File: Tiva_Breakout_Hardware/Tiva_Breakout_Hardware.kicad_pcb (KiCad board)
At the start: 2 copper layers, 146.1 x 69.8 mm, 61 parts, among them U1 TM4C129E_Launchpad

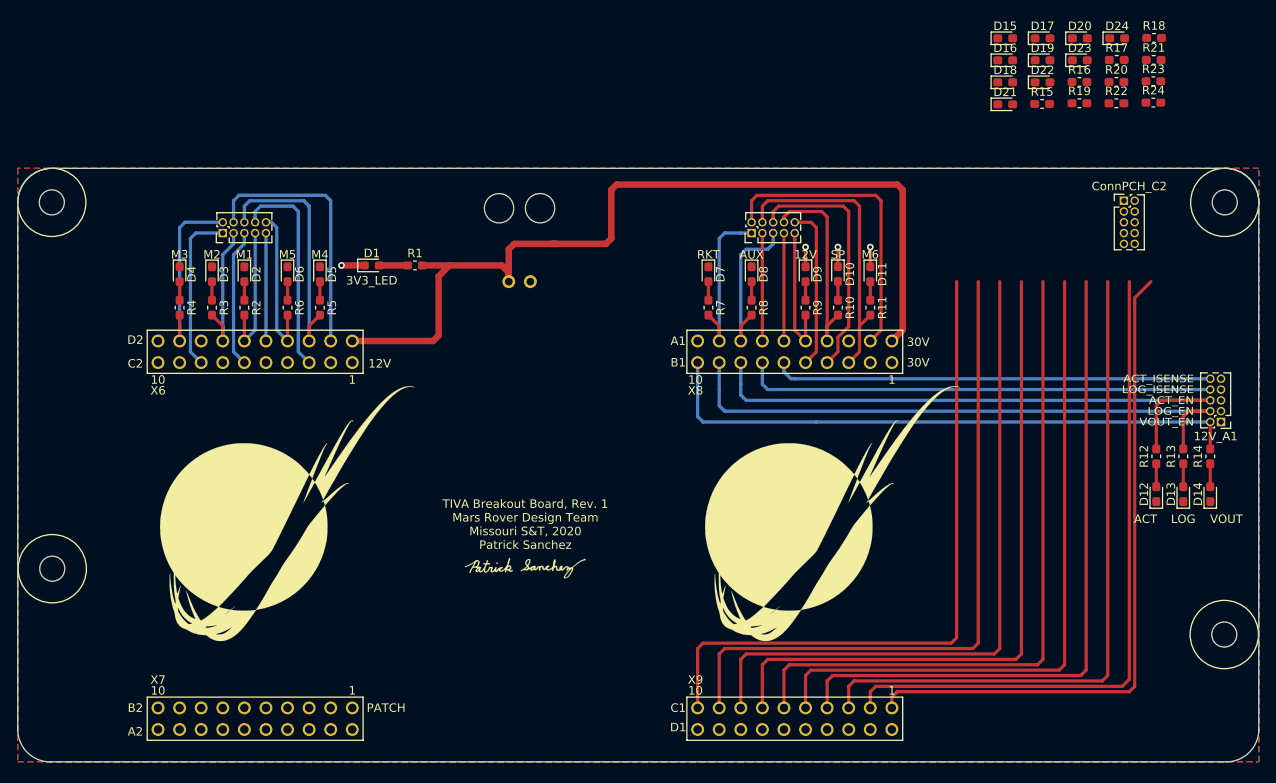
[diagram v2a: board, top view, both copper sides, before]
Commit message: Finished all wiring and LEDs, need resizing and silkscreen
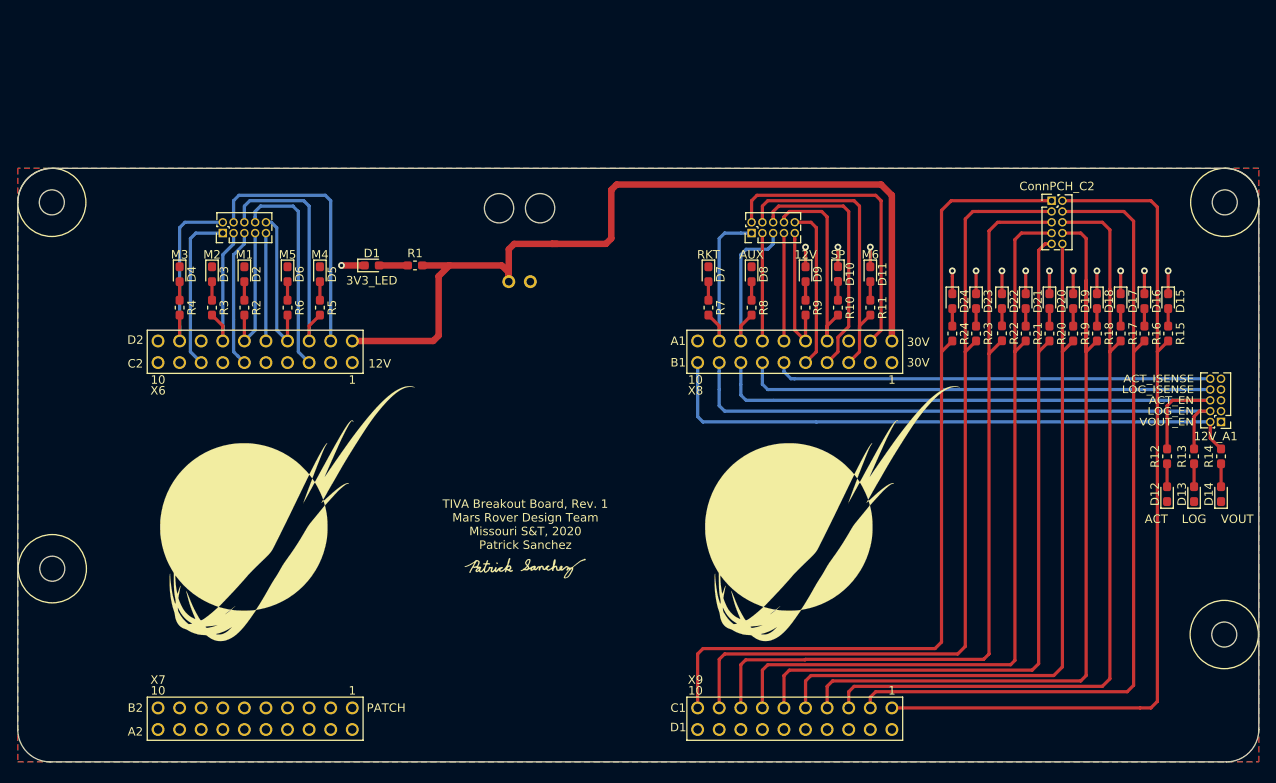
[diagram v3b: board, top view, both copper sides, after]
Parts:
- moved D24 36.5 mm to (194.5, 90.9), turned to 270 degrees
- moved D15 36.4 mm to (219.9, 90.9), turned to 270 degrees
- moved R23 36.3 mm to (197.3, 94.8), turned to 270 degrees
- moved R24 36.0 mm to (194.5, 94.8), turned to 270 degrees
- moved R21 35.5 mm to (203.1, 94.8), turned to 270 degrees
- moved R18 35.4 mm to (211.5, 94.8), turned to 270 degrees
- moved D16 32.7 mm to (217.1, 90.9), turned to 270 degrees
- moved D17 32.3 mm to (214.3, 90.9), turned to 270 degrees
- moved R17 32.2 mm to (214.3, 94.8), turned to 270 degrees
- moved D20 31.1 mm to (205.9, 90.9), turned to 270 degrees
- moved D23 30.9 mm to (197.3, 90.9), turned to 270 degrees
- moved R15 30.8 mm to (219.9, 94.8), turned to 270 degrees
- moved R20 30.6 mm to (205.9, 94.8), turned to 270 degrees
- moved R16 30.6 mm to (217.1, 94.8), turned to 270 degrees
- moved R22 30.2 mm to (200.4, 94.7), turned to 270 degrees
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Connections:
- ConnPCH_C2 pad 1: PATCH10_EN -> PATCH1_EN
- ConnPCH_C2 pad 10: PATCH5_EN -> PATCH6_EN
- ConnPCH_C2 pad 2: PATCH1_EN -> PATCH10_EN
- ConnPCH_C2 pad 3: PATCH9_EN -> PATCH2_EN
- ConnPCH_C2 pad 4: PATCH2_EN -> PATCH9_EN
- ConnPCH_C2 pad 5: PATCH8_EN -> PATCH3_EN
- ConnPCH_C2 pad 6: PATCH3_EN -> PATCH8_EN
- ConnPCH_C2 pad 7: PATCH7_EN -> PATCH4_EN
- ConnPCH_C2 pad 8: PATCH4_EN -> PATCH7_EN
- ConnPCH_C2 pad 9: PATCH6_EN -> PATCH5_EN
- R15 pad 2: PATCH1_EN -> PATCH10_EN
- R16 pad 2: PATCH2_EN -> PATCH9_EN
- R17 pad 2: PATCH3_EN -> PATCH8_EN
- R18 pad 2: PATCH4_EN -> PATCH7_EN
- R19 pad 2: PATCH5_EN -> PATCH6_EN
- R20 pad 2: PATCH6_EN -> PATCH5_EN
- R21 pad 2: PATCH7_EN -> PATCH4_EN
- R22 pad 2: PATCH8_EN -> PATCH3_EN
- R23 pad 2: PATCH9_EN -> PATCH2_EN
- R24 pad 2: PATCH10_EN -> PATCH1_EN
- U1 pad PF1: PATCH1_EN -> PATCH10_EN
- U1 pad PF2: PATCH2_EN -> PATCH9_EN
- U1 pad PF3: PATCH3_EN -> PATCH8_EN
- U1 pad PG0: PATCH4_EN -> PATCH7_EN
- U1 pad PL0: PATCH7_EN -> PATCH4_EN
- U1 pad PL1: PATCH8_EN -> PATCH3_EN
- U1 pad PL2: PATCH9_EN -> PATCH2_EN
- U1 pad PL3: PATCH10_EN -> PATCH1_EN
- U1 pad PL4: PATCH5_EN -> PATCH6_EN
- U1 pad PL5: PATCH6_EN -> PATCH5_EN
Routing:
- net GND: track 9.62 -> 36.6 mm, vias 4 -> 14
- net PATCH10_EN: track 79.9 -> 103.0 mm
- net PATCH1_EN: track 78.8 -> 101.7 mm
- net PATCH7_EN: track 79.9 -> 98.2 mm
- net PATCH9_EN: track 79.9 -> 98.1 mm
- net PATCH2_EN: track 79.8 -> 97.9 mm
- net PATCH3_EN: track 79.9 -> 94.5 mm
- net PATCH8_EN: track 79.9 -> 93.9 mm
- net PATCH4_EN: track 79.9 -> 90.6 mm
- net PATCH5_EN: track 79.9 -> 86.6 mm
- net PATCH6_EN: track 79.9 -> 85.7 mm
- net +3V3: track 106.7 -> 104.5 mm
- net Net-(D24-Pad2): track 0.00 -> 2.06 mm
- net Net-(D23-Pad2): track 0.00 -> 2.06 mm
- net Net-(D21-Pad2): track 0.00 -> 2.06 mm
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
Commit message: Finished layout, minus some silk screen stuff
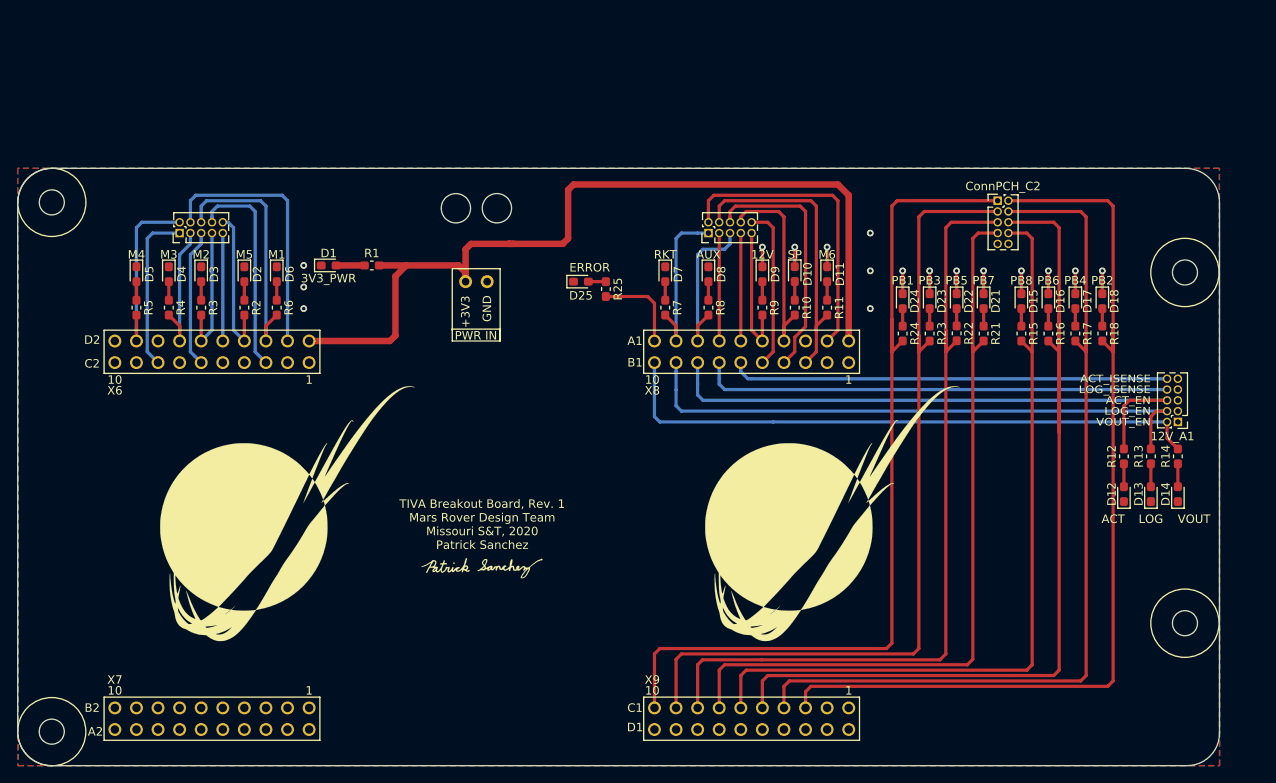
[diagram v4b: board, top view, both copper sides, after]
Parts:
- removed D19, D20: 3V3_LED, LED_SMD:LED_0603_1608Metric_Pad1.05x0.95mm_HandSolder
- removed R19, R20: 330, Resistor_SMD:R_0603_1608Metric_Pad1.05x0.95mm_HandSolder
- removed the REF** at (88.6, 122.4)
- removed the REF** at (226.5, 130.2)
- added D25: 3V3_LED, LED_SMD:LED_0603_1608Metric_Pad1.05x0.95mm_HandSolder, F.Cu at (150.8, 88.6)
- added R25: 330, Resistor_SMD:R_0603_1608Metric_Pad1.05x0.95mm_HandSolder, F.Cu at (153.7, 89.5)
- added REF**: 4_40_Hole, MRDT_Drill_Holes:4_40_Hole, F.Cu at (221.9, 128.8)
- added REF**: 4_40_Hole, MRDT_Drill_Holes:4_40_Hole, F.Cu at (221.9, 87.6)
- moved REF** 162.1 mm to (84.5, 145.6), turned to 0 degrees
- moved D5 21.6 mm to (98.5, 87.8)
- moved R5 21.6 mm to (98.5, 91.7)
- moved D15 17.3 mm to (202.6, 90.9)
- moved R15 17.3 mm to (202.6, 94.8)
- moved D16 11.3 mm to (205.8, 90.9)
- moved R16 11.3 mm to (205.8, 94.8)
- moved ConnPCH_C2 6.35 mm to (199.8, 79.1)
- moved D24 5.84 mm to (188.7, 90.9)
- moved R24 5.84 mm to (188.7, 94.8)
- moved D23 5.46 mm to (191.8, 90.9)
- moved R23 5.46 mm to (191.8, 94.8)
- moved D17 5.33 mm to (209.0, 90.9)
- moved D22 5.33 mm to (195.0, 90.9)
- moved R17 5.33 mm to (209.0, 94.8)
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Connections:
- net PATCH1_EN renamed PB1_EN
- net PATCH2_EN renamed PB3_EN
- net PATCH3_EN renamed PB5_EN
- net PATCH4_EN renamed PB7_EN
- Conn30V_L1 pad 10: M5_EN -> M1_EN
- Conn30V_L1 pad 2: M3_EN -> M4_EN
- Conn30V_L1 pad 3: M2_EN -> M3_EN
- Conn30V_L1 pad 6: M4_EN -> M5_EN
- Conn30V_L1 pad 7: M1_EN -> M2_EN
- Conn30V_R1 pad 10: 12V_ISENSE -> SP_ISENSE
- Conn30V_R1 pad 2: M6_ISENSE -> RKT_ISENSE
- Conn30V_R1 pad 3: RKT_ISENSE -> AUX_ISENSE
- Conn30V_R1 pad 6: SP_ISENSE -> M6_ISENSE
- Conn30V_R1 pad 7: AUX_ISENSE -> 12V_ISENSE
- ConnPCH_C2 pad 10: PATCH6_EN -> GND
- ConnPCH_C2 pad 2: PATCH10_EN -> PB2_EN
- ConnPCH_C2 pad 4: PATCH9_EN -> PB4_EN
- ConnPCH_C2 pad 6: PATCH8_EN -> PB6_EN
- ConnPCH_C2 pad 8: PATCH7_EN -> PB8_EN
- ConnPCH_C2 pad 9: PATCH5_EN -> GND
- R15 pad 2: PATCH10_EN -> PB8_EN
- R16 pad 2: PATCH9_EN -> PB6_EN
- R17 pad 2: PATCH8_EN -> PB4_EN
- R18 pad 2: PATCH7_EN -> PB2_EN
- U1 pad PB3: Net-(U1-PadPB3) -> ERROR
- U1 pad PD3: RKT_ISENSE -> AUX_ISENSE
- U1 pad PD5: M1_EN -> M2_EN
- U1 pad PE1: SP_ISENSE -> M6_ISENSE
- U1 pad PE2: 12V_ISENSE -> SP_ISENSE
- U1 pad PE4: M6_ISENSE -> RKT_ISENSE
- U1 pad PE5: AUX_ISENSE -> 12V_ISENSE
- U1 pad PF1: PATCH10_EN -> Net-(U1-PadPF1)
- U1 pad PF2: PATCH9_EN -> Net-(U1-PadPF2)
- U1 pad PF3: PATCH8_EN -> PB2_EN
- U1 pad PG0: PATCH7_EN -> PB4_EN
- U1 pad PL4: PATCH6_EN -> PB6_EN
- U1 pad PL5: PATCH5_EN -> PB8_EN
- U1 pad PN5: M3_EN -> M4_EN
- U1 pad PP0: M4_EN -> M5_EN
- U1 pad PP1: M5_EN -> M1_EN
- U1 pad PQ0: M2_EN -> M3_EN
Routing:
- net PB6_EN: track 0.00 -> 117.1 mm
- net PB2_EN: track 0.00 -> 111.4 mm
- net PB4_EN: track 0.00 -> 105.1 mm
- net PATCH10_EN: track 103.0 -> 0.00 mm
- net PATCH7_EN: track 98.2 -> 0.00 mm
- net PATCH9_EN: track 98.1 -> 0.00 mm
- net PATCH8_EN: track 93.9 -> 0.00 mm
- net PB8_EN: track 0.00 -> 93.6 mm
- net PATCH5_EN: track 86.6 -> 0.00 mm
- net PATCH6_EN: track 85.7 -> 0.00 mm
- net RKT_ISENSE: track 12.7 -> 35.3 mm
- net M5_EN: track 18.4 -> 29.5 mm
- net ERROR: track 0.00 -> 10.5 mm
- net SP_ISENSE: track 29.5 -> 19.2 mm
- net GND: track 36.6 -> 28.5 mm, vias 14 -> 17
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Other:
- board size 146.1 x 69.8 mm -> 141.4 x 70.3 mm
- board text added: "3V3_PWR"
- board text added: "ERROR"
- board text added: "PB1"
- board text added: "PB2"
- board text added: "PB3"
- board text added: "PB4"
- board text added: "PB5"
- board text added: "PB6"
- board text added: "PB7"
- board text added: "PB8"
- board text removed: "30V"
- board text removed: "3V3_LED"
- board text removed: "ACT_CRRT"
- board text removed: "ACT_CTRL"
- board text removed: "LOG_CRRT"
- board text removed: "LOG_CTRL"
- board text removed: "PATCH"

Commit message: Added pulldown resistors & LED colors
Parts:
- added R19: 10k, Resistor_SMD:R_0603_1608Metric_Pad1.05x0.95mm_HandSolder, F.Cu at (188.7, 121.4)
- added R20: 10k, Resistor_SMD:R_0603_1608Metric_Pad1.05x0.95mm_HandSolder, F.Cu at (191.8, 121.4)
- added R26: 10k, Resistor_SMD:R_0603_1608Metric_Pad1.05x0.95mm_HandSolder, F.Cu at (195.0, 121.4)
- added R27: 10k, Resistor_SMD:R_0603_1608Metric_Pad1.05x0.95mm_HandSolder, F.Cu at (198.2, 121.4)
- added R28: 10k, Resistor_SMD:R_0603_1608Metric_Pad1.05x0.95mm_HandSolder, F.Cu at (212.2, 121.4)
- added R29: 10k, Resistor_SMD:R_0603_1608Metric_Pad1.05x0.95mm_HandSolder, F.Cu at (209.0, 121.4)
- added R30: 10k, Resistor_SMD:R_0603_1608Metric_Pad1.05x0.95mm_HandSolder, F.Cu at (205.8, 121.4)
- added R31: 10k, Resistor_SMD:R_0603_1608Metric_Pad1.05x0.95mm_HandSolder, F.Cu at (202.6, 121.4)
- D1: value 3V3_LED -> GRN
- D10, D11, D12, D13, D14, D15, D16, D17, D18, D2, D21, D22, D23, D24, D3, D4, D5, D6, D7, D8, D9: value 3V3_LED -> BLU
- D25: value 3V3_LED -> RED
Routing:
- net GND: track 28.5 -> 45.0 mm, vias 17 -> 25
- net PB8_EN: track 93.6 -> 95.4 mm
- net PB7_EN: track 90.0 -> 91.8 mm
- net PB4_EN: track 105.1 -> 106.9 mm
- net PB3_EN: track 98.9 -> 100.6 mm
- net PB2_EN: track 111.4 -> 113.2 mm
- net PB1_EN: track 104.6 -> 106.4 mm
- net PB6_EN: track 117.1 -> 118.9 mm
- net PB5_EN: track 95.7 -> 97.5 mm

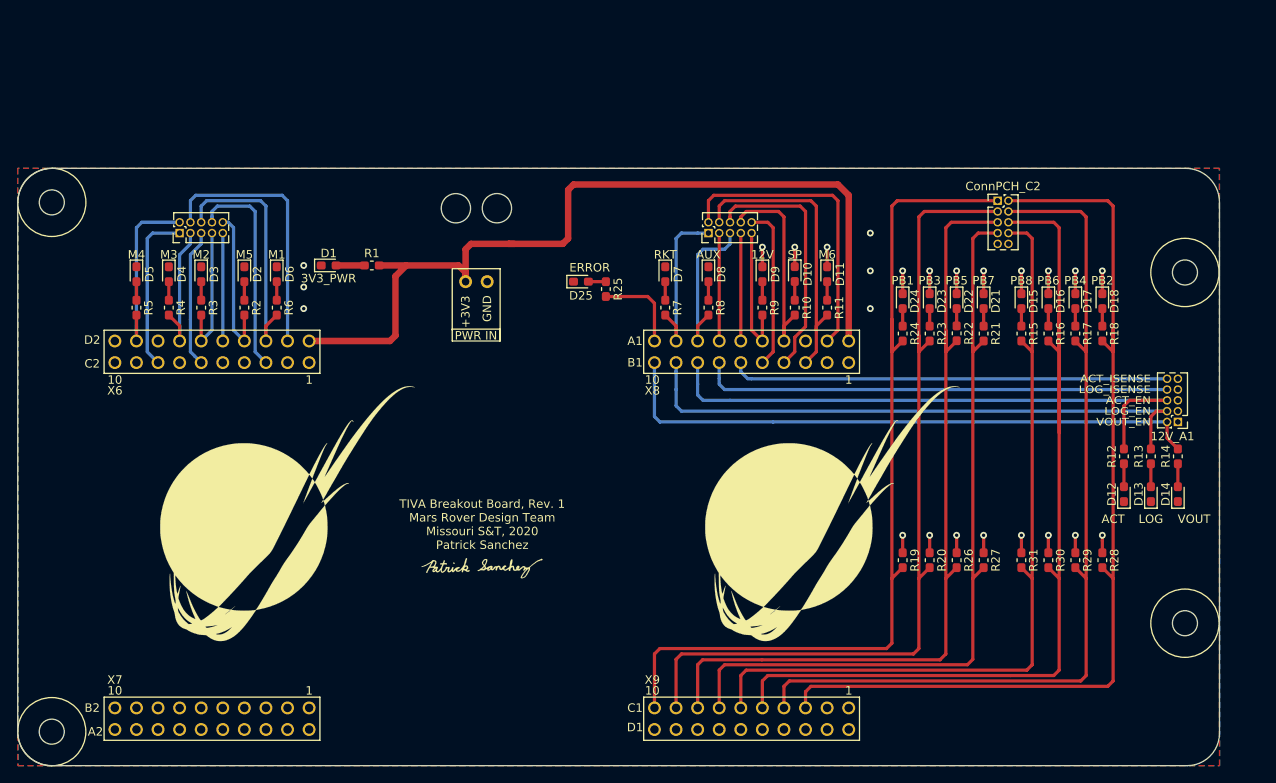
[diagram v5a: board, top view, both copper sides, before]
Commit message: Added pullup resistors and pin labels
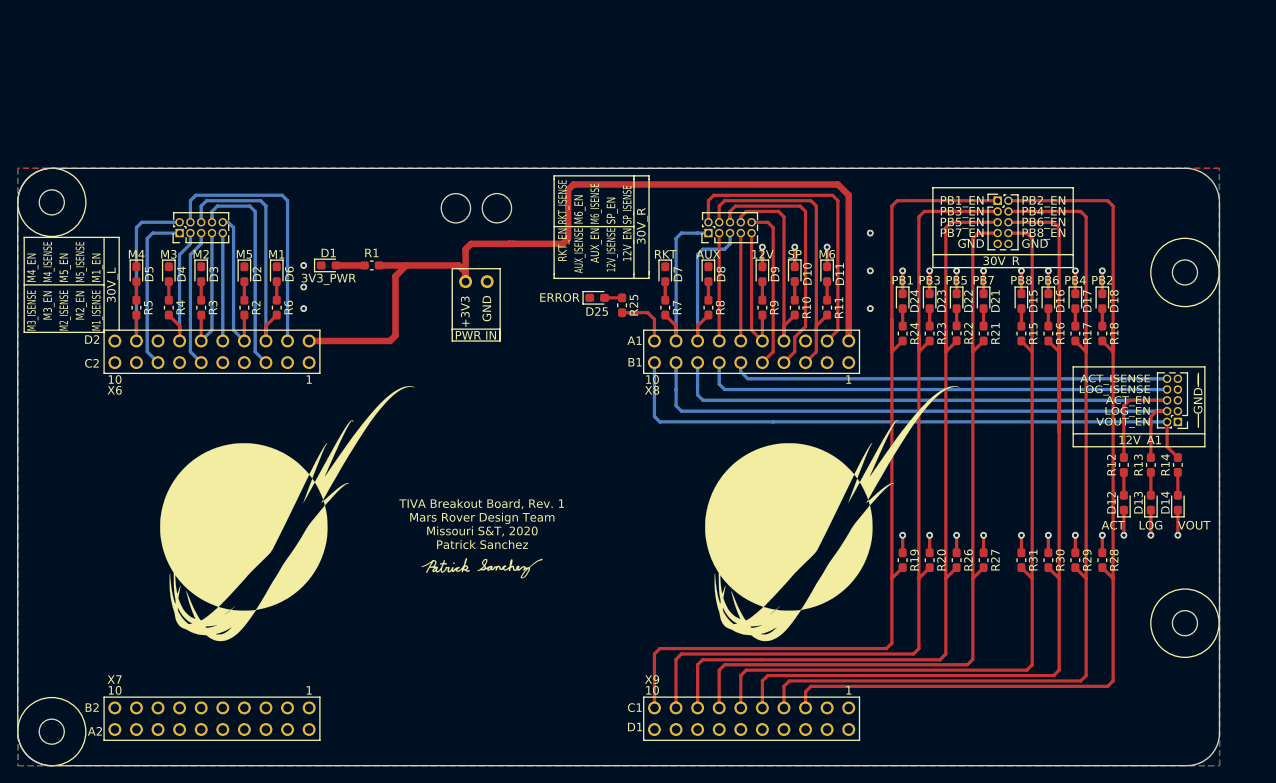
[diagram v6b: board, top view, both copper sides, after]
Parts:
- moved R25 2.69 mm to (155.7, 91.4)
- moved D25 2.69 mm to (152.7, 90.6)
- moved D12 1.02 mm to (214.7, 114.7)
- moved D13 1.02 mm to (217.9, 114.7)
- moved D14 1.02 mm to (221.1, 114.7)
- moved R12 1.02 mm to (214.7, 110.2)
- moved R13 1.02 mm to (217.9, 110.2)
- moved R14 1.02 mm to (221.1, 110.2)
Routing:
- net GND: track 45.0 -> 53.8 mm, vias 25 -> 28
- net ERROR: track 10.5 -> 6.68 mm
- net VOUT_EN: track 70.6 -> 71.7 mm
- net LOG_EN: track 69.1 -> 70.1 mm
- net ACT_EN: track 69.7 -> 70.8 mm
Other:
- board text added: "12V_EN"
- board text added: "12V_ISENSE"
- board text added: "30V_L"
- board text added: "30V_R"
- board text added: "AUX_EN"
- board text added: "AUX_ISENSE"
- board text added: "M1_EN"
- board text added: "M1_ISENSE"
- board text added: "M2_EN"
- board text added: "M2_ISENSE"
- board text added: "M3_EN"
- board text added: "M3_ISENSE"
- board text added: "M4_EN"
- board text added: "M4_ISENSE"
- board text added: "M5_EN"
- board text added: "M5_ISENSE"
- board text added: "M6_EN"
- board text added: "M6_ISENSE"
- board text added: "PB1_EN"
- board text added: "PB2_EN"
- board text added: "PB3_EN"
- board text added: "PB4_EN"
- board text added: "PB5_EN"
- board text added: "PB6_EN"
- board text added: "PB7_EN"
- board text added: "PB8_EN"
- board text added: "RKT_EN"
- board text added: "RKT_ISENSE"
- board text added: "SP_EN"
- board text added: "SP_ISENSE"
- board text removed: "PATCH PANEL"
- board text removed: "PCH_1"
- board text removed: "PCH_2"
- board text removed: "PCH_3"
- board text removed: "PCH_4"
- board text removed: "PCH_5"
- board text removed: "PCH_6"
- board text removed: "PCH_7"
- board text removed: "PCH_8"
- board text removed: "TEST_LED1"
- board text removed: "TEST_LED2"
